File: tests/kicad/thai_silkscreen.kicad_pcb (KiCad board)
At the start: 2 copper layers, 90 x 46 mm, 0 parts

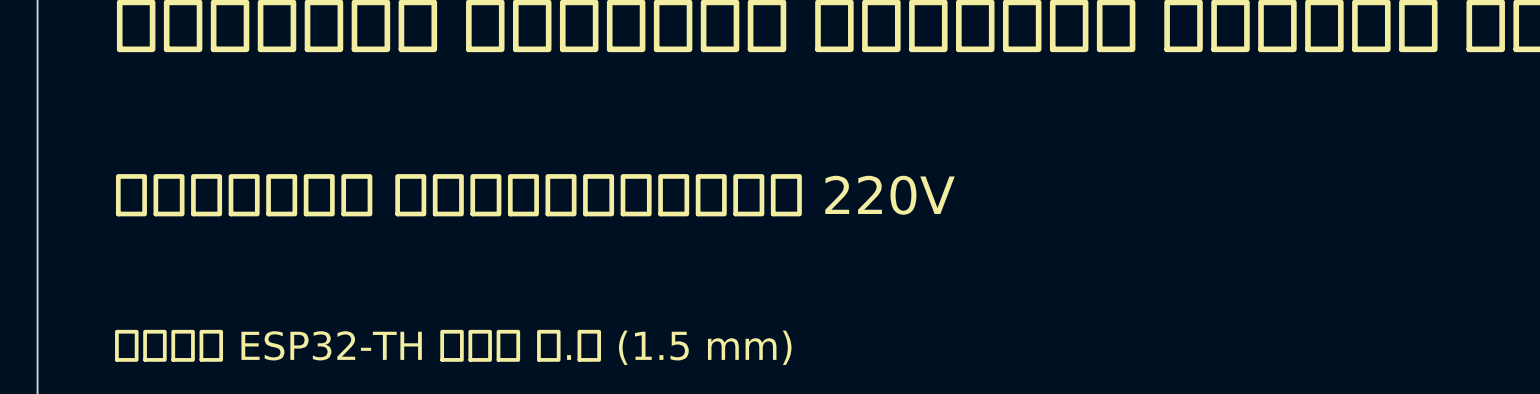
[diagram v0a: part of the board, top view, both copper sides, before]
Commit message: Fix review findings, verified on real KiCad 8.0.9/9.0.9/10.0.6
- presets no longer override net-class clearance (safety); silk rule only vs pads
- run_checks proves .kicad_dru loaded with a canary rule (exit 2 if KiCad ignored it)
- mains add-on: Mains_HV class (6.4 mm), functional L-N, symmetric conditions;
  integration test proves the rules fire on KiCad 9 and 10
- export: --rot mirrored on bottom side, BOM/board cross-check, refuse unannotated
  parts, warn on Thai text with KiCad 8 (drops vowels/tone marks), UTF-8 I/O,
  numeric Windows version sort, Flatpak-safe temp dir, no stale STEP
- docs: Thai wording (220 V is not ไฟฟ้าแรงสูง), sources, verified Thai findings

Co-Authored-By: Claude Opus 5.5 <noreply@anthropic.com>
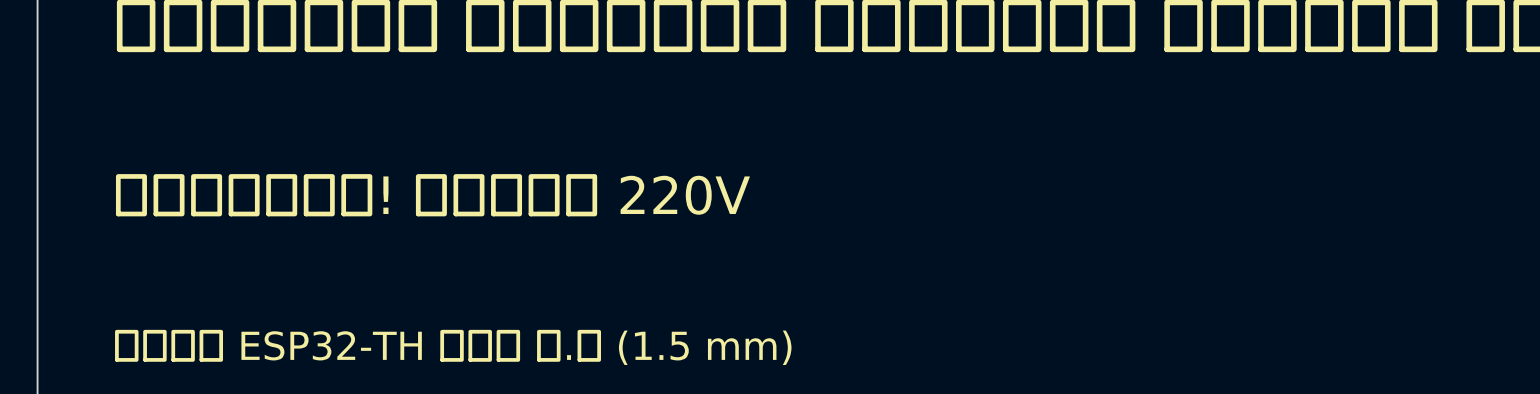
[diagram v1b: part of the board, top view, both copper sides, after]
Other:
- board text added: "อันตราย! ไฟฟ้า 220V"
- board text removed: "อันตราย ไฟฟ้าแรงสูง 220V"
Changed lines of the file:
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@@
 		(effects (font (face "Sarabun") (size 2.5 2.5) (thickness 0.3)) (justify left))
 	)
-	(gr_text "อันตราย ไฟฟ้าแรงสูง 220V"
+	(gr_text "อันตราย! ไฟฟ้า 220V"
 		(at 4 18 0)
 		(layer "F.SilkS")
